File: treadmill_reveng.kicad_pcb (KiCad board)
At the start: 2 copper layers, 12 parts, among them K1 HK19F-5V-SHG, K2 HK19F-5V-SHG, Q1 IKW50N60H3, U1 L293D, U2 L7805

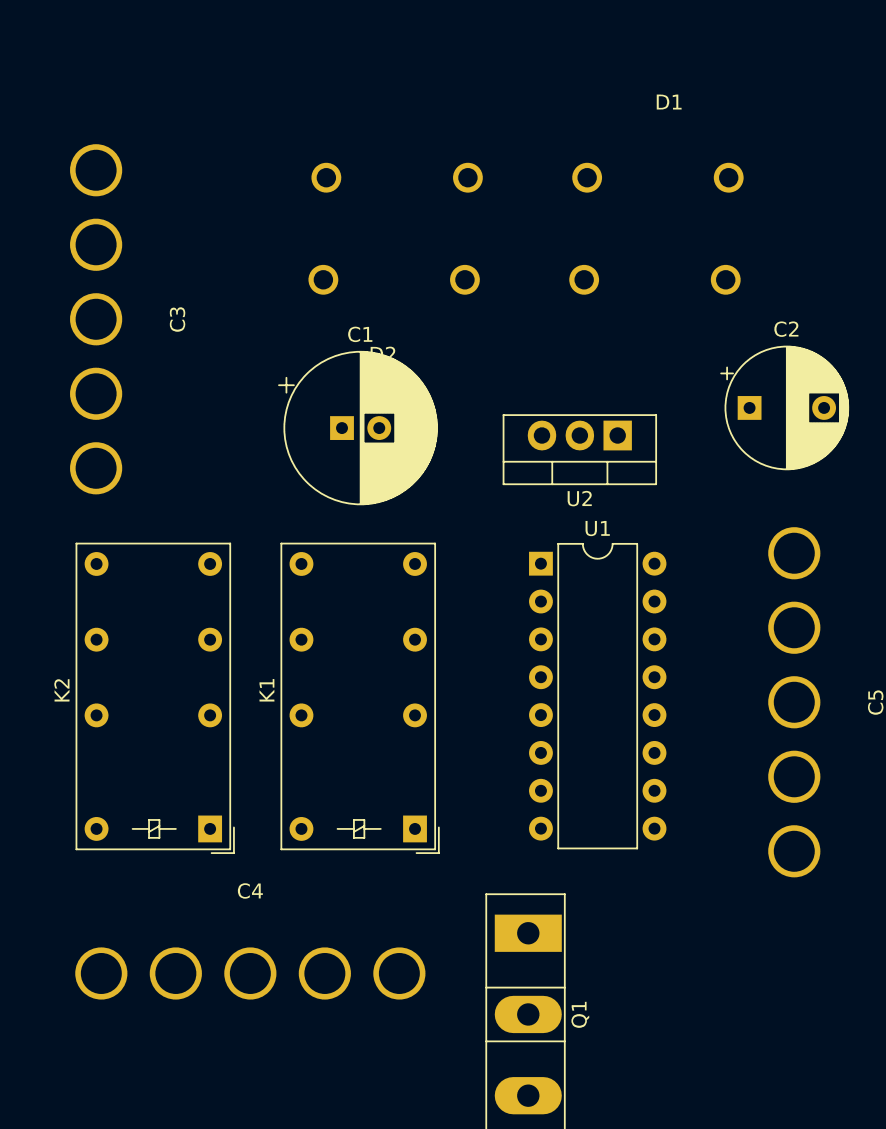
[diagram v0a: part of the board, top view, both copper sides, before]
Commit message: added pull down resistor
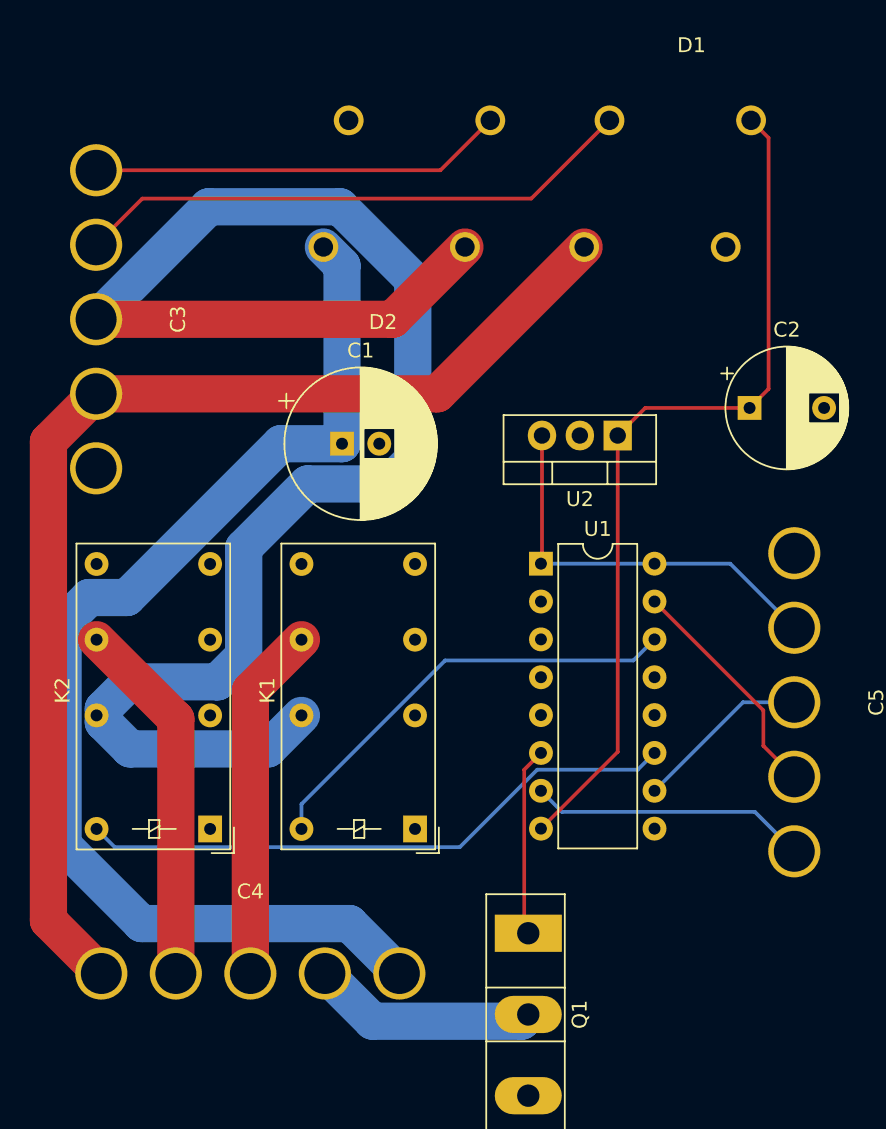
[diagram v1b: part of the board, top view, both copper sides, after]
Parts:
- moved D1 4.13 mm to (83.0, -18.1)
- moved D2 2.20 mm to (62.4, -4.55)
- moved C1 1.05 mm to (59.6, 6.15)
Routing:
- net AC220VLive: track 0.00 -> 113.1 mm
- net AC220N: track 0.00 -> 78.5 mm
- net DC220Vpostive: track 0.00 -> 78.4 mm
- net DC12Vpostive: track 0.00 -> 58.4 mm
- net Net-(K2-PadA2): track 0.00 -> 40.6 mm
- net AC12vN: track 0.00 -> 37.9 mm
- net Net-(K1-PadA2): track 0.00 -> 29.9 mm
- net AC12vLive: track 0.00 -> 27.8 mm
- net DC5v: track 0.00 -> 27.4 mm
- net ACMotorRed: track 0.00 -> 24.6 mm
- net ACMotorBlack: track 0.00 -> 23.8 mm
- net CONTROL_DCMotorNegative: track 0.00 -> 18.7 mm
- net CONTROL_ACMotorBlack: track 0.00 -> 15.6 mm
- net DcMotorNegative: track 0.00 -> 15.2 mm
- net Net-(Q1-Pad1): track 0.00 -> 12.7 mm
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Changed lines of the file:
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@@
     (thickness 1.6)
     (drawings 0)
-    (tracks 0)
+    (tracks 76)
     (zones 0)
     (modules 12)
@@
   )
   (setup
-    (last_trace_width 0.25)
+    (last_trace_width 2.5)
+    (user_trace_width 2.5)
+    (user_trace_width 5)
     (trace_clearance 0.2)
     (zone_clearance 0.508)
@@
   )
   (module Capacitor_THT:CP_Radial_D10.0mm_P2.50mm (layer F.Cu)
-    (at 59.6 5.1)
+    (at 59.6 6.15)
     (descr "CP, Radial series, Radial, pin pitch=2.50mm, , diameter=10mm, Electrolytic Capacitor")
     (tags "CP Radial series Radial pin pitch 2.50mm  diameter 10mm Electrolytic Capacitor")
@@
   )
   (module GBJ5010:GBJ5010 (layer F.Cu)
-    (at 81.55 -14.2 180)
+    (at 83.05 -18.05 180)
     (fp_text reference D1 (at 0 2.54) (layer F.SilkS)
       (effects (font (size 1 1) (thickness 0.15)))
@@
   )
   (module GBJ5010:GBJ5010 (layer F.Cu)
-    (at 62.35 -2.35)
+    (at 62.35 -4.55)
     (fp_text reference D2 (at 0 2.54) (layer F.SilkS)
       (effects (font (size 1 1) (thickness 0.15)))
@@
     )
   )
+  (segment (start 55.489998 6.15) (end 59.6 6.15) (width 2.5) (layer B.Cu) (net 1))
+  (segment (start 45.169997 16.470001) (end 55.489998 6.15) (width 2.5) (layer B.Cu) (net 1))
+  (segment (start 42.629997 16.470001) (end 45.169997 16.470001) (width 2.5) (layer B.Cu) (net 1))
+  (segment (start 40.879999 33.080001) (end 40.879999 18.219999) (width 2.5) (layer B.Cu) (net 1))
+  (segment (start 40.879999 18.219999) (end 42.629997 16.470001) (width 2.5) (layer B.Cu) (net 1))
+  (segment (start 46.149998 38.35) (end 40.879999 33.080001) (width 2.5) (layer B.Cu) (net 1))
+  (segment (start 60.1 38.35) (end 46.149998 38.35) (width 2.5) (layer B.Cu) (net 1))
+  (segment (start 63.45 41.7) (end 60.1 38.35) (width 2.5) (layer B.Cu) (net 1))
+  (segment (start 59.6 -5.8) (end 58.35 -7.05) (width 2.5) (layer B.Cu) (net 1))
+  (segment (start 59.6 6.15) (end 59.6 -5.8) (width 2.5) (layer B.Cu) (net 1))
+  (segment (start 88.225001 2.474999) (end 86.95 3.75) (width 0.25) (layer F.Cu) (net 3))
+  (segment (start 88.225001 -14.374999) (end 88.225001 2.474999) (width 0.25) (layer F.Cu) (net 3))
+  (segment (start 87.05 -15.55) (end 88.225001 -14.374999) (width 0.25) (layer F.Cu) (net 3))
+  (segment (start 79.95 3.75) (end 78.1 5.6) (width 0.25) (layer F.Cu) (net 3))
+  (segment (start 86.95 3.75) (end 79.95 3.75) (width 0.25) (layer F.Cu) (net 3))
+  (segment (start 78.1 26.83) (end 72.95 31.98) (width 0.25) (layer F.Cu) (net 3))
+  (segment (start 78.1 5.6) (end 78.1 26.83) (width 0.25) (layer F.Cu) (net 3))
+  (segment (start 66 2.8) (end 75.85 -7.05) (width 2.5) (layer F.Cu) (net 5))
+  (segment (start 43.1 2.8) (end 66 2.8) (width 2.5) (layer F.Cu) (net 5))
+  (segment (start 39.899999 6.000001) (end 43.1 2.8) (width 2.5) (layer F.Cu) (net 5))
+  (segment (start 39.899999 38.149999) (end 39.899999 6.000001) (width 2.5) (layer F.Cu) (net 5))
+  (segment (start 43.45 41.7) (end 39.899999 38.149999) (width 2.5) (layer F.Cu) (net 5))
+  (segment (start 63 -2.2) (end 67.85 -7.05) (width 2.5) (layer F.Cu) (net 6))
+  (segment (start 43.1 -2.2) (end 63 -2.2) (width 2.5) (layer F.Cu) (net 6))
+  (segment (start 45.380001 22.129999) (end 43.580009 23.929991) (width 2.5) (layer B.Cu) (net 6))
+  (segment (start 43.580009 24.830009) (end 45.380001 26.630001) (width 2.5) (layer B.Cu) (net 6))
+  (segment (start 51.250003 22.129999) (end 45.380001 22.129999) (width 2.5) (layer B.Cu) (net 6))
+  (segment (start 54.629999 26.630001) (end 56.88 24.38) (width 2.5) (layer B.Cu) (net 6))
+  (segment (start 43.580009 23.929991) (end 43.580009 24.830009) (width 2.5) (layer B.Cu) (net 6))
+  (segment (start 53.000001 20.380001) (end 51.250003 22.129999) (width 2.5) (layer B.Cu) (net 6))
+  (segment (start 53.000001 13.139999) (end 53.000001 20.380001) (width 2.5) (layer B.Cu) (net 6))
+  (segment (start 57.28999 8.85001) (end 53.000001 13.139999) (width 2.5) (layer B.Cu) (net 6))
+  (segment (start 62.729992 8.85001) (end 57.28999 8.85001) (width 2.5) (layer B.Cu) (net 6))
+  (segment (start 64.350001 7.230001) (end 62.729992 8.85001) (width 2.5) (layer B.Cu) (net 6))
+  (segment (start 64.350001 -4.868389) (end 64.350001 7.230001) (width 2.5) (layer B.Cu) (net 6))
+  (segment (start 45.380001 26.630001) (end 54.629999 26.630001) (width 2.5) (layer B.Cu) (net 6))
+  (segment (start 59.468381 -9.750009) (end 64.350001 -4.868389) (width 2.5) (layer B.Cu) (net 6))
+  (segment (start 50.650009 -9.750009) (end 59.468381 -9.750009) (width 2.5) (layer B.Cu) (net 6))
+  (segment (start 43.1 -2.2) (end 50.650009 -9.750009) (width 2.5) (layer B.Cu) (net 6))
+  (segment (start 77.55 -15.55) (end 72.3 -10.3) (width 0.25) (layer F.Cu) (net 7))
+  (segment (start 46.2 -10.3) (end 43.1 -7.2) (width 0.25) (layer F.Cu) (net 7))
+  (segment (start 72.3 -10.3) (end 46.2 -10.3) (width 0.25) (layer F.Cu) (net 7))
+  (segment (start 66.2 -12.2) (end 69.55 -15.55) (width 0.25) (layer F.Cu) (net 8))
+  (segment (start 43.1 -12.2) (end 66.2 -12.2) (width 0.25) (layer F.Cu) (net 8))
+  (segment (start 48.45 24.62) (end 43.13 19.3) (width 2.5) (layer F.Cu) (net 9))
+  (segment (start 48.45 41.7) (end 48.45 24.62) (width 2.5) (layer F.Cu) (net 9))
+  (segment (start 53.45 22.73) (end 56.88 19.3) (width 2.5) (layer F.Cu) (net 10))
+  (segment (start 53.45 41.7) (end 53.45 22.73) (width 2.5) (layer F.Cu) (net 10))
+  (segment (start 61.650001 44.900001) (end 58.45 41.7) (width 2.5) (layer B.Cu) (net 11))
+  (segment (start 71.649999 44.900001) (end 61.650001 44.900001) (width 2.5) (layer B.Cu) (net 11))
+  (segment (start 72.1 44.45) (end 71.649999 44.900001) (width 2.5) (layer B.Cu) (net 11))
+  (segment (start 74.364999 30.854999) (end 72.95 29.44) (width 0.25) (layer B.Cu) (net 12))
+  (segment (start 87.304999 30.854999) (end 74.364999 30.854999) (width 0.25) (layer B.Cu) (net 12))
+  (segment (start 89.95 33.5) (end 87.304999 30.854999) (width 0.25) (layer B.Cu) (net 12))
+  (segment (start 87.874999 24.044999) (end 80.57 16.74) (width 0.25) (layer F.Cu) (net 13))
+  (segment (start 87.874999 26.424999) (end 87.874999 24.044999) (width 0.25) (layer F.Cu) (net 13))
+  (segment (start 89.95 28.5) (end 87.874999 26.424999) (width 0.25) (layer F.Cu) (net 13))
+  (segment (start 86.51 23.5) (end 80.57 29.44) (width 0.25) (layer B.Cu) (net 14))
+  (segment (start 89.95 23.5) (end 86.51 23.5) (width 0.25) (layer B.Cu) (net 14))
+  (segment (start 72.95 14.2) (end 80.57 14.2) (width 0.25) (layer B.Cu) (net 15))
+  (segment (start 85.65 14.2) (end 89.95 18.5) (width 0.25) (layer B.Cu) (net 15))
+  (segment (start 80.57 14.2) (end 85.65 14.2) (width 0.25) (layer B.Cu) (net 15))
+  (segment (start 73.02 14.13) (end 72.95 14.2) (width 0.25) (layer F.Cu) (net 15))
+  (segment (start 73.02 5.6) (end 73.02 14.13) (width 0.25) (layer F.Cu) (net 15))
+  (segment (start 56.88 30.334998) (end 56.88 32) (width 0.25) (layer B.Cu) (net 16))
+  (segment (start 66.519999 20.694999) (end 56.88 30.334998) (width 0.25) (layer B.Cu) (net 16))
+  (segment (start 79.155001 20.694999) (end 66.519999 20.694999) (width 0.25) (layer B.Cu) (net 16))
+  (segment (start 80.57 19.28) (end 79.155001 20.694999) (width 0.25) (layer B.Cu) (net 16))
+  (segment (start 79.444999 28.025001) (end 80.57 26.9) (width 0.25) (layer B.Cu) (net 17))
+  (segment (start 72.699997 28.025001) (end 79.444999 28.025001) (width 0.25) (layer B.Cu) (net 17))
+  (segment (start 67.499997 33.225001) (end 72.699997 28.025001) (width 0.25) (layer B.Cu) (net 17))
+  (segment (start 44.355001 33.225001) (end 67.499997 33.225001) (width 0.25) (layer B.Cu) (net 17))
+  (segment (start 43.13 32) (end 44.355001 33.225001) (width 0.25) (layer B.Cu) (net 17))
+  (segment (start 71.824999 28.025001) (end 72.95 26.9) (width 0.25) (layer F.Cu) (net 20))
+  (segment (start 71.824999 38.724999) (end 71.824999 28.025001) (width 0.25) (layer F.Cu) (net 20))
+  (segment (start 72.1 39) (end 71.824999 38.724999) (width 0.25) (layer F.Cu) (net 20))
 )

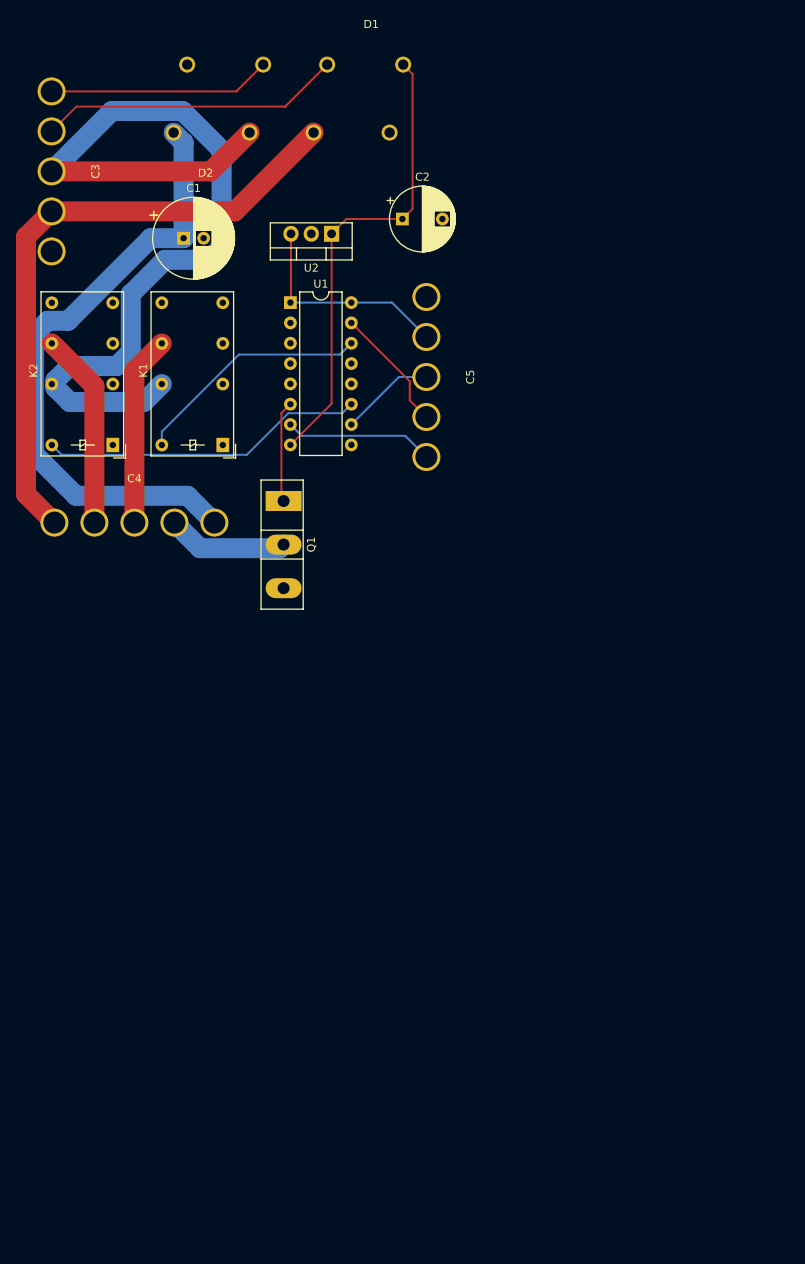
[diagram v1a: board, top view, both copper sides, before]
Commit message: copper fill
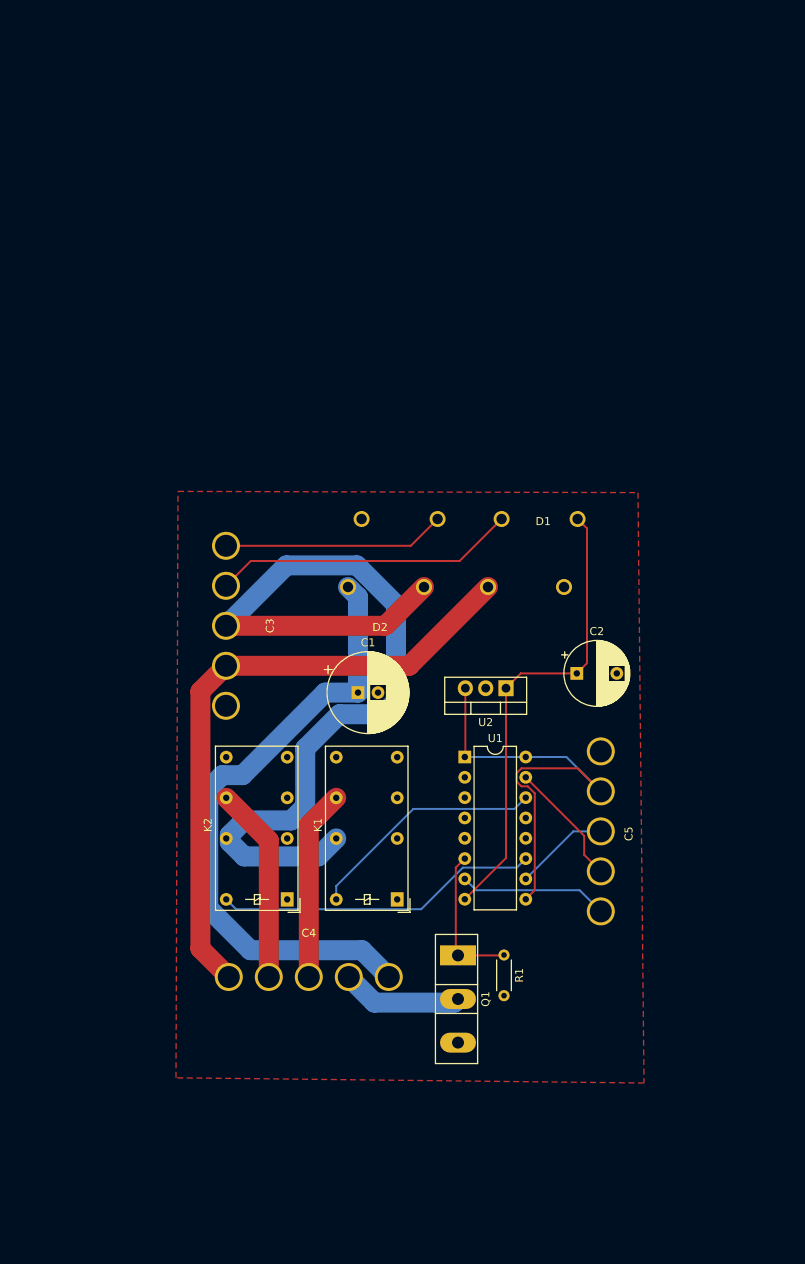
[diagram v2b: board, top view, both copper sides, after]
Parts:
- added R1: 10k, Resistor_THT:R_Axial_DIN0204_L3.6mm_D1.6mm_P5.08mm_Horizontal, F.Cu at (99.7, 95.8)
- moved C1 60.8 mm to (81.4, 63.0)
- moved C3 60.8 mm to (69.9, 54.6)
- moved C2 60.8 mm to (108.8, 60.5)
- moved C4 60.8 mm to (75.2, 93.5)
- moved C5 60.8 mm to (116.8, 80.3)
- moved D1 60.8 mm to (104.8, 38.8)
- moved D2 60.8 mm to (84.2, 52.2)
- moved K1 60.8 mm to (86.3, 88.8)
- moved K2 60.8 mm to (72.5, 88.8)
- moved Q1 60.8 mm to (93.9, 95.8)
- moved U1 60.8 mm to (94.8, 71.0)
- moved U2 60.8 mm to (99.9, 62.4)
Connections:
- K1 pad 22: ACMotorBlack -> Net-(K1-Pad22)
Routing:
- net DC5v: track 27.4 -> 57.0 mm
- net Net-(Q1-Pad1): track 12.7 -> 18.5 mm
- added copper zone on F.Cu, net DCGND

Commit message: new netlist with correct sizes
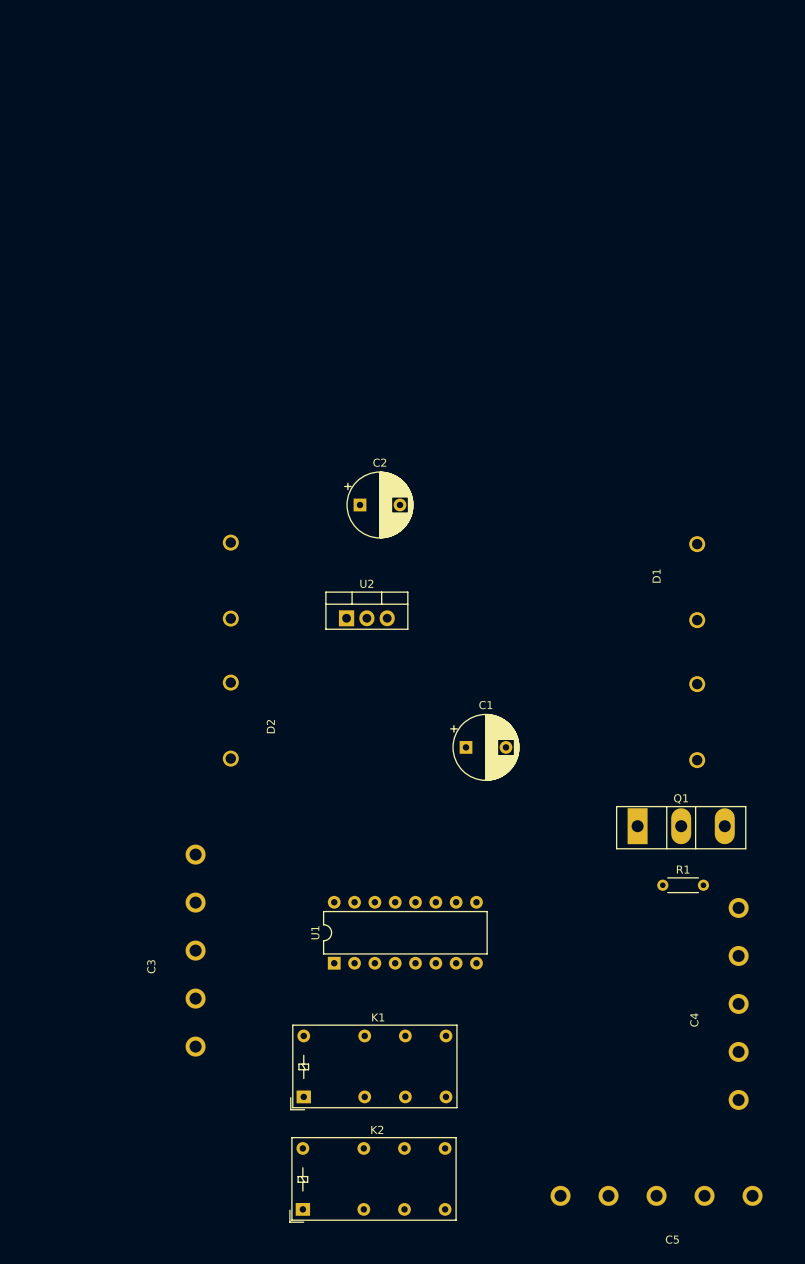
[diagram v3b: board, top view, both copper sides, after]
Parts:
- C1: footprint Capacitor_THT:CP_Radial_D10.0mm_P2.50mm -> Capacitor_THT:CP_Radial_D8.0mm_P5.00mm
- moved C5 50.7 mm to (120.7, 130.9), turned to 0 degrees
- moved C4 49.8 mm to (124.0, 103.9), turned to 270 degrees
- moved C3 44.8 mm to (56.1, 97.2), turned to 270 degrees
- moved K2 38.8 mm to (74.5, 127.5), turned to 0 degrees
- moved C2 34.3 mm to (81.7, 39.5)
- moved U1 30.5 mm to (78.4, 96.8), turned to 90 degrees
- moved Q1 27.7 mm to (116.3, 79.7), turned to 0 degrees
- moved K1 27.3 mm to (74.6, 113.5), turned to 0 degrees
- moved D2 22.0 mm to (68.0, 67.2), turned to 90 degrees
- moved U2 21.8 mm to (80.0, 53.7), turned to 0 degrees
- moved R1 21.7 mm to (119.5, 87.0), turned to 0 degrees
- moved D1 19.1 mm to (121.3, 48.4), turned to 270 degrees
- moved C1 15.1 mm to (94.9, 69.8)
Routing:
- net AC220VLive: track 113.1 -> 0.00 mm
- net AC220N: track 78.5 -> 0.00 mm
- net DC220Vpostive: track 78.4 -> 0.00 mm
- net DC12Vpostive: track 58.4 -> 0.00 mm
- net DC5v: track 57.0 -> 0.00 mm
- net Net-(K2-PadA2): track 40.6 -> 0.00 mm
- net AC12vN: track 37.9 -> 0.00 mm
- net Net-(K1-PadA2): track 29.9 -> 0.00 mm
- net AC12vLive: track 27.8 -> 0.00 mm
- net ACMotorRed: track 24.6 -> 0.00 mm
- net ACMotorBlack: track 23.8 -> 0.00 mm
- net CONTROL_DCMotorNegative: track 18.7 -> 0.00 mm
- net Net-(Q1-Pad1): track 18.5 -> 0.00 mm
- net CONTROL_ACMotorBlack: track 15.6 -> 0.00 mm
- net DcMotorNegative: track 15.2 -> 0.00 mm
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- removed copper zone on F.Cu, net DCGND
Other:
- net class Default: clearance 0.2 -> 0.25
- rule trace_clearance: 0.2 -> 0.25
- rule trace_min: 0.2 -> 0.25

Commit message: new placement
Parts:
- moved D1 62.9 mm to (66.7, 79.6)
- moved C4 23.9 mm to (100.1, 105.5)
- moved C3 19.2 mm to (54.0, 78.1)

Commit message: rev2 routing
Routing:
- net DC5v: track 0.00 -> 119.8 mm, vias 0 -> 1
- net AC220N: track 0.00 -> 95.7 mm, vias 0 -> 1
- net DC12Vpostive: track 0.00 -> 77.6 mm
- net AC220VLive: track 0.00 -> 73.5 mm
- net DC220Vpostive: track 0.00 -> 55.9 mm
- net CONTROL_ACMotorBlack: track 0.00 -> 50.5 mm
- net CONTROL_ACMotorRed: track 0.00 -> 47.3 mm
- net CONTROL_DCMotorNegative: track 0.00 -> 47.1 mm
- net Net-(Q1-Pad1): track 0.00 -> 43.1 mm
- net Net-(K2-PadA2): track 0.00 -> 38.9 mm, vias 0 -> 1
- net DcMotorNegative: track 0.00 -> 24.8 mm
- net ACMotorRed: track 0.00 -> 22.2 mm
- net Net-(K1-PadA2): track 0.00 -> 20.4 mm
- net AC12vLive: track 0.00 -> 12.3 mm
- net AC12vN: track 0.00 -> 11.5 mm
- added copper zone on B.Cu, net DCGND
- added copper zone on F.Cu, net DCGND
